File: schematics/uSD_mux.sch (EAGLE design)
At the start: 15 parts

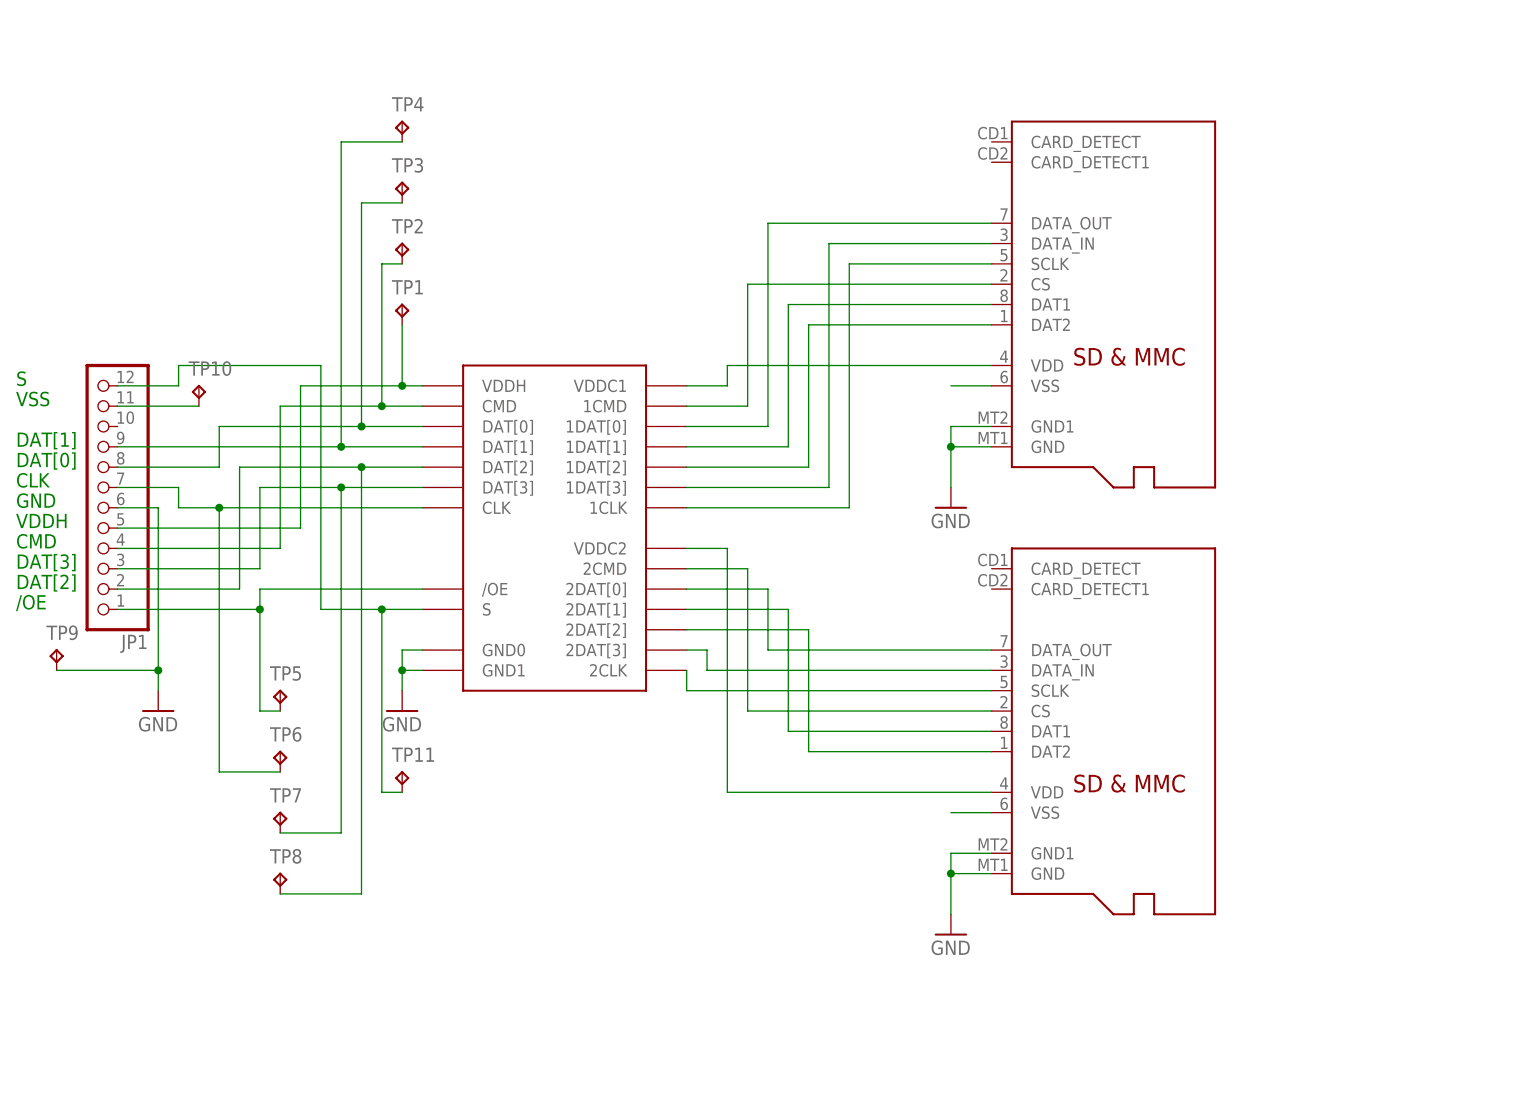
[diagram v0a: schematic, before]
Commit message: Updated uSD mux board
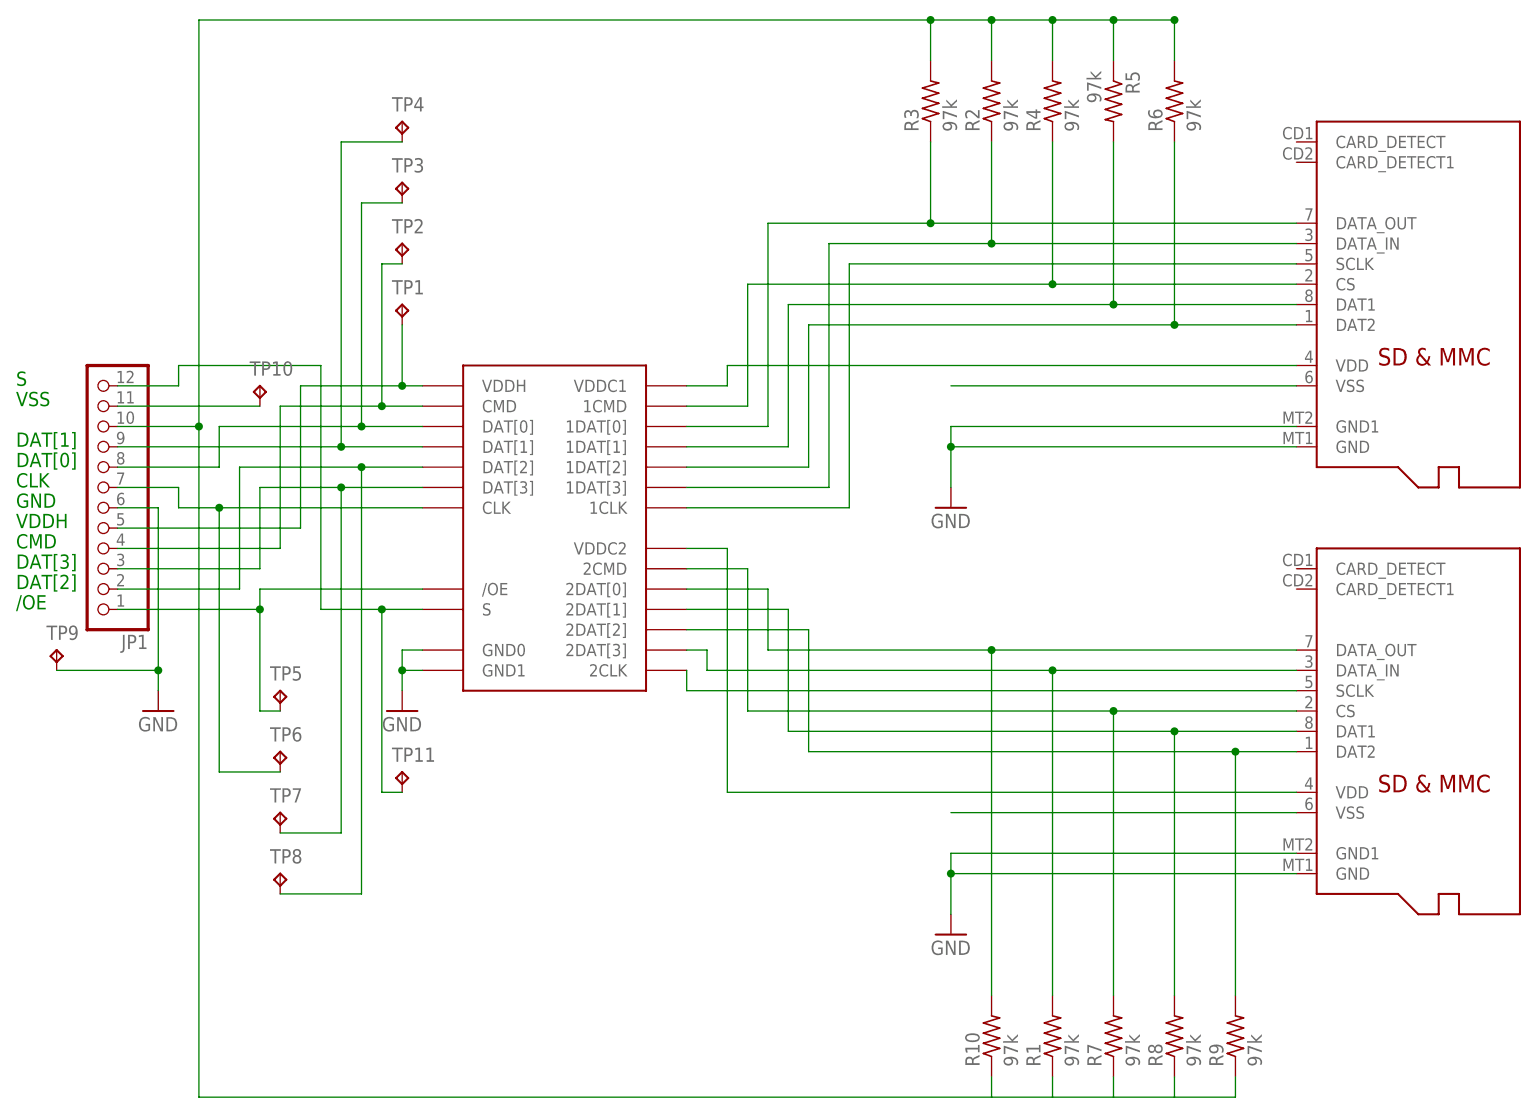
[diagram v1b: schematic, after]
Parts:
- added R1, R10, R2, R3, R4, R5, R6, R7, R8, R9: 97k, rcl:R-US_R0805
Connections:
- new net N$1: JP1.10, R1.1, R10.1, R2.2, R3.2, R4.2, R5.1, R6.2, R7.1, R8.1, R9.1
- net N$10: now also R8.2
- net N$11: now also R9.2
- net N$12: now also R1.2
- net N$2: now also R4.1
- net N$3: now also R3.1
- net N$4: now also R5.2
- net N$5: now also R6.1
- net N$6: now also R2.1
- net N$8: now also R7.2
- net N$9: now also R10.2
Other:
- moved on the sheet: TP10

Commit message: Updated uSD mux sch/brd files
Added decoupling capacitors, labeled +3.6V connection on 12 pin
connector.
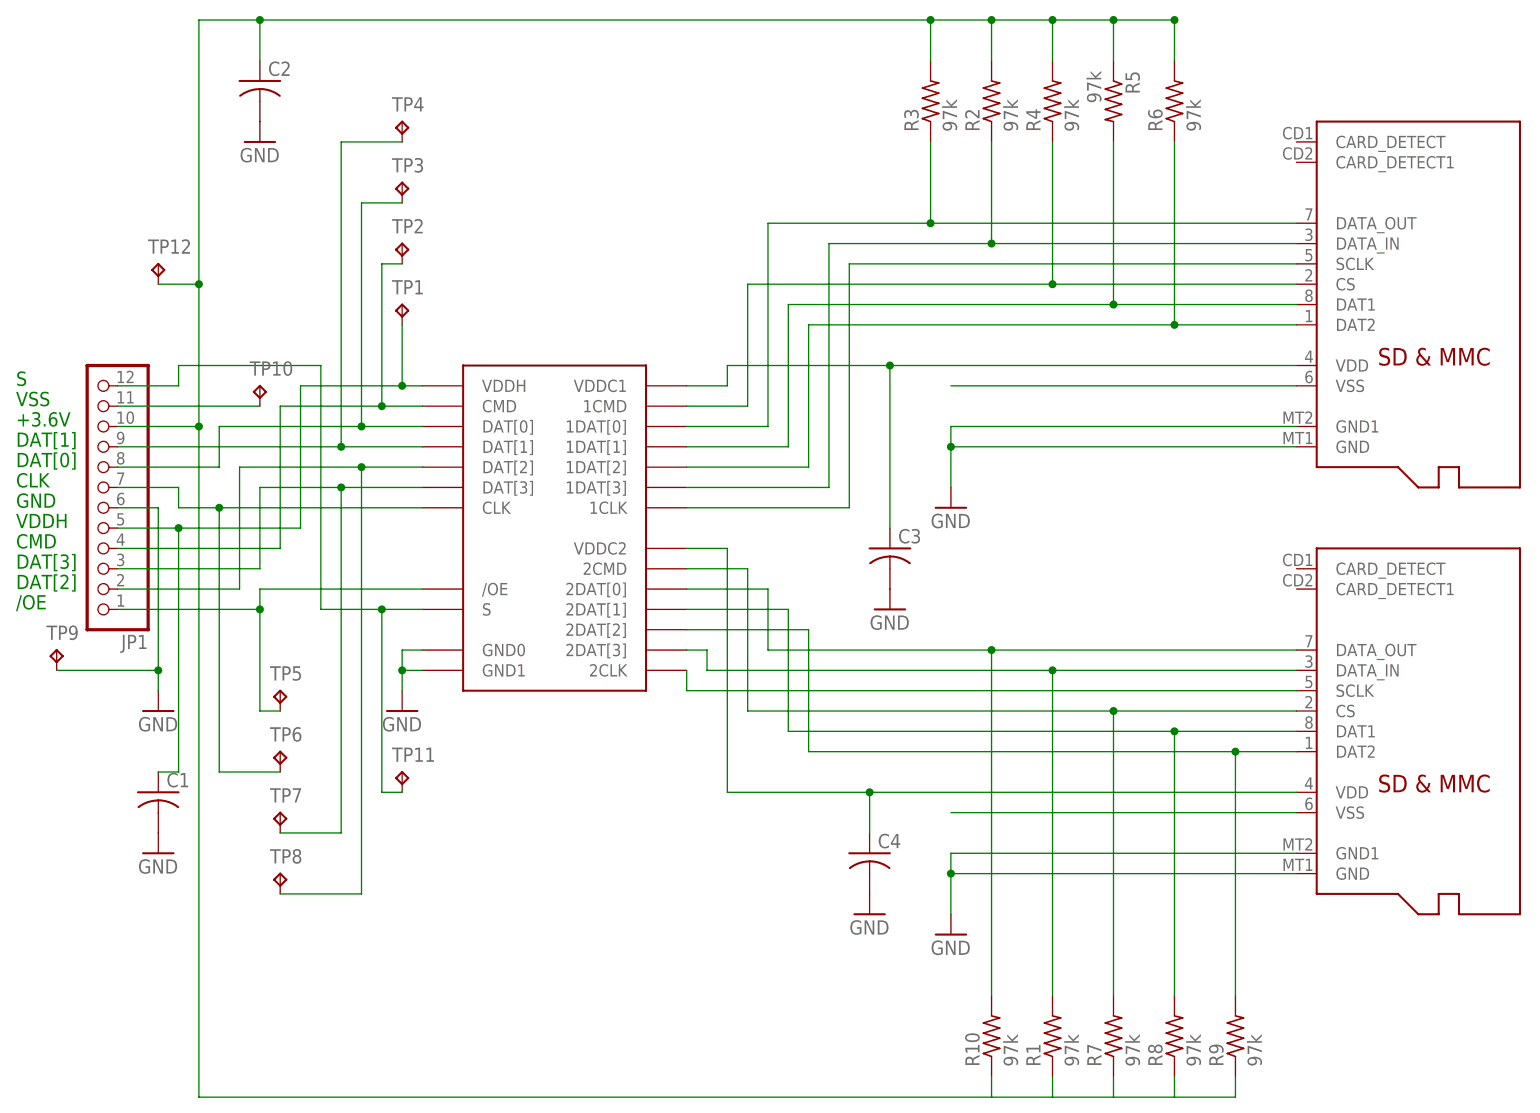
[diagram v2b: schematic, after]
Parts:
- added C1, C2, C3, C4: (no value), rcl:C-USC0805
- added TP12: TPTP20R, testpad:TPTP20R
- renumbered U$1 to +3.6V
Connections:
- net GND: now also C1.2, C2.2, C3.2, C4.2
- net N$1: now also C2.1, TP12.TP
- net VDDC1: now also C3.1
- net VDDC2: now also C4.1
- net VDDH: now also C1.1
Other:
- note added: "+3.6V"

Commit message: Breakout boards for MUX and uSD socket, updated mux+uSD schematic
Built individual breakout boards for MUX chip and uSD socket.
Discovered errors in MUX and uSD integrated board and updated
schematic--ripped up wrong connections in .brd file but did not bother
rerouting traces since this board will most likely not be fabbed again.
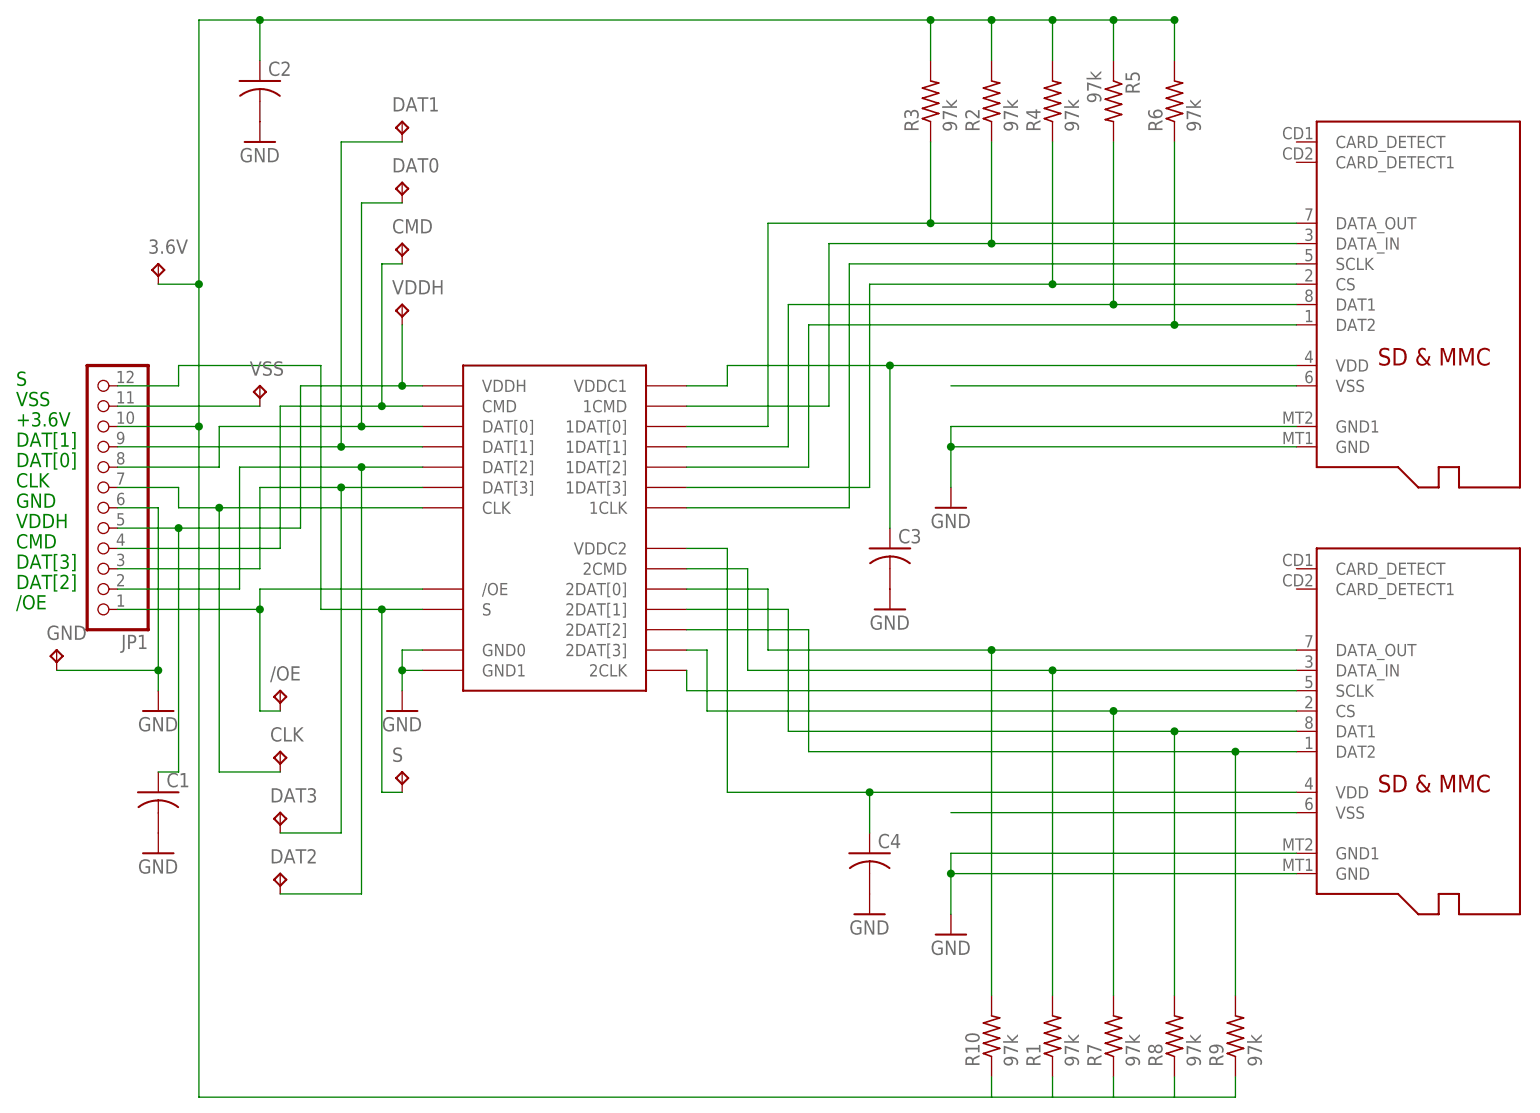
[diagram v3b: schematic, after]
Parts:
- renumbered TP1 to VDDH, TP10 to VSS, TP11 to S, TP12 to 3.6V, TP2 to CMD, TP3 to DAT0, TP4 to DAT1, TP5 to /OE, TP6 to CLK, TP7 to DAT3, TP8 to DAT2, TP9 to GND, U$2 to USD1, U$3 to USD2
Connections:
- net N$1 renamed +3.6
- removed net N$2: +3.6V.1CMD, R4.1, USD1.CS
- new net N$1: +3.6V.1DAT[3], R4.1, USD1.CS
- net N$12: now also +3.6V.2CMD; no longer +3.6V.2DAT[3]
- net N$6: now also +3.6V.1CMD; no longer +3.6V.1DAT[3]
- net N$8: now also +3.6V.2DAT[3]; no longer +3.6V.2CMD
